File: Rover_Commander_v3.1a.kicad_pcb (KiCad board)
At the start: 2 copper layers, 77 x 42 mm, 73 parts, among them Q1 Crystal KX-7 25MHz, Q2 Crystal KX-7 25MHz, U1 RTL8201CP, U2 L7805ABD2T-TR, U3 H1102NLT, U4 LD1117S33TR_SOT223, U5 STM32F107RCTx, U6 TJA1040T, U7 M95160-WMN6TP

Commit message: fix swd connector, reversed GND and POWER +3.3V
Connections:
- XP2 pad 1: /+3V3_STM -> GND
- XP2 pad 4: GND -> /+3V3_STM
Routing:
- net GND: track 489.3 -> 497.2 mm, vias 13 -> 15
- net /+3V3_STM: track 79.9 -> 83.5 mm
- net (no net): vias 0 -> 1

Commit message: switch to my library https://github.com/Zulljon/zpkl.git
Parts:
- U2: footprint TO254P1542X460-3N -> zulljon:TO254P1542X460-3N
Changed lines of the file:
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@@
     )
   )
-  (module TO254P1542X460-3N (layer F.Cu)
+  (module zulljon:TO254P1542X460-3N (layer F.Cu)
     (at 127.712 115.316 180)
     (descr D2PAK_STD_ST)
     (tags "Integrated Circuit")
     (attr smd)
-    (fp_text reference U2 (at 0.712 6.316 180) (layer F.SilkS)
+    (fp_text reference U2 (at 0 0 180) (layer F.SilkS)
       (effects (font (size 1.27 1.27) (thickness 0.254)))
     )
@@
     (fp_line (start 0 0.5) (end 0 -0.5) (layer Dwgs.User) (width 0.05))
     (fp_line (start -0.5 0) (end 0.5 0) (layer Dwgs.User) (width 0.05))
-    (fp_line (start -2.708 5.1) (end 6.442 5.1) (layer Dwgs.User) (width 0.1))
-    (fp_line (start 6.442 5.1) (end 6.442 -5.1) (layer Dwgs.User) (width 0.1))
-    (fp_line (start 6.442 -5.1) (end -2.708 -5.1) (layer Dwgs.User) (width 0.1))
-    (fp_line (start -2.708 -5.1) (end -2.708 5.1) (layer Dwgs.User) (width 0.1))
-    (fp_line (start 6.442 5.1) (end 6.861 5.1) (layer Dwgs.User) (width 0.1))
-    (fp_line (start 6.861 5.1) (end 7.712 4.157) (layer Dwgs.User) (width 0.1))
-    (fp_line (start 7.712 4.157) (end 7.712 -4.157) (layer Dwgs.User) (width 0.1))
-    (fp_line (start 7.712 -4.157) (end 6.861 -5.1) (layer Dwgs.User) (width 0.1))
-    (fp_line (start 6.861 -5.1) (end 6.442 -5.1) (layer Dwgs.User) (width 0.1))
+    (fp_line (start -2.708 5.1) (end 6.442 5.1) (layer F.Fab) (width 0.1))
+    (fp_line (start 6.442 5.1) (end 6.442 -5.1) (layer F.Fab) (width 0.1))
+    (fp_line (start 6.442 -5.1) (end -2.708 -5.1) (layer F.Fab) (width 0.1))
+    (fp_line (start -2.708 -5.1) (end -2.708 5.1) (layer F.Fab) (width 0.1))
+    (fp_line (start 6.442 5.1) (end 6.861 5.1) (layer F.Fab) (width 0.1))
+    (fp_line (start 6.861 5.1) (end 7.712 4.157) (layer F.Fab) (width 0.1))
+    (fp_line (start 7.712 4.157) (end 7.712 -4.157) (layer F.Fab) (width 0.1))
+    (fp_line (start 7.712 -4.157) (end 6.861 -5.1) (layer F.Fab) (width 0.1))
+    (fp_line (start 6.861 -5.1) (end 6.442 -5.1) (layer F.Fab) (width 0.1))
     (fp_line (start -0.4 5.1) (end -4.1 5.1) (layer F.SilkS) (width 0.2))
     (fp_line (start -4.1 5.1) (end -4.1 -5.1) (layer F.SilkS) (width 0.2))

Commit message: add transient voltage suppression diods on CAN
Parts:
- added D7: SMAJ33CA-TR, Diodes_SMD:D_SMA, F.Cu at (114.5, 97.0)
- added D8: SMAJ33CA-TR, Diodes_SMD:D_SMA, F.Cu at (114.5, 104.5)
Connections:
- U1 pad 27: (no net) -> Net-(U1-Pad27)
- U5 pad 20: (no net) -> Net-(U5-Pad20)
- U5 pad 28: (no net) -> Net-(U5-Pad28)
- U5 pad 35: (no net) -> Net-(U5-Pad35)
- U5 pad 36: (no net) -> Net-(U5-Pad36)
- U5 pad 37: (no net) -> Net-(U5-Pad37)
- U5 pad 38: (no net) -> Net-(U5-Pad38)
- U5 pad 4: (no net) -> Net-(U5-Pad4)
- U5 pad 40: (no net) -> Net-(U5-Pad40)
- U5 pad 41: (no net) -> Net-(U5-Pad41)
- U5 pad 43: (no net) -> Net-(U5-Pad43)
- U5 pad 54: (no net) -> Net-(U5-Pad54)
- U5 pad 55: (no net) -> Net-(U5-Pad55)
- U5 pad 56: (no net) -> Net-(U5-Pad56)
- U5 pad 59: (no net) -> Net-(U5-Pad59)
- U5 pad 60: (no net) -> Net-(U5-Pad60)
- U5 pad 62: (no net) -> Net-(U5-Pad62)
- U5 pad 7: (no net) -> Net-(U5-Pad7)
- U5 pad 8: (no net) -> Net-(U5-Pad8)
- U7 pad 3: (no net) -> Net-(U7-Pad3)
- U7 pad 7: (no net) -> Net-(U7-Pad7)
- XP3 pad 9: (no net) -> /OBD2_ETH_ACT
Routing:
- net GND: track 497.2 -> 519.5 mm
- net /OBD2_CAN_H: track 6.88 -> 14.8 mm
- net /OBD2_CAN_L: track 13.1 -> 20.4 mm
- net Net-(C22-Pad1): track 24.3 -> 25.6 mm

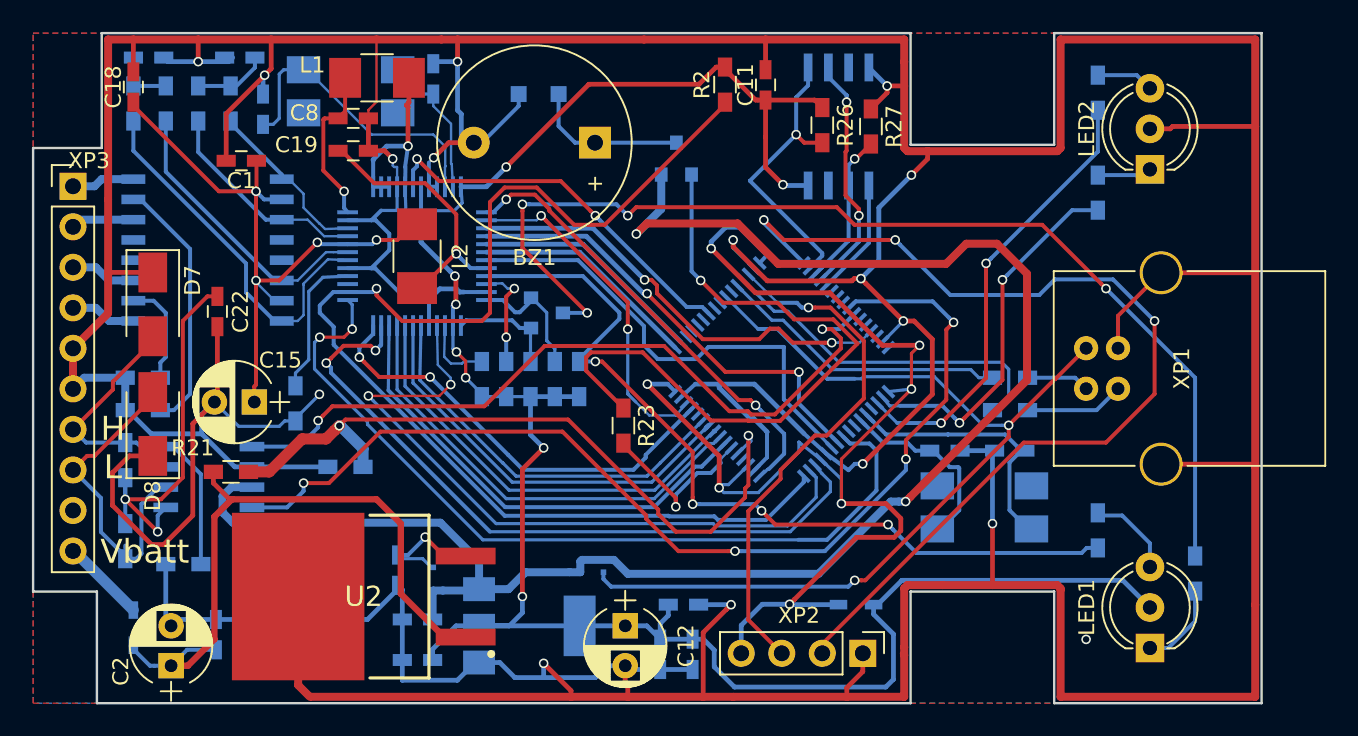
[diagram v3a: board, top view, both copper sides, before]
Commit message: fix crystals package, add thermo-pads to voltage regulator, fix usb like differential pair
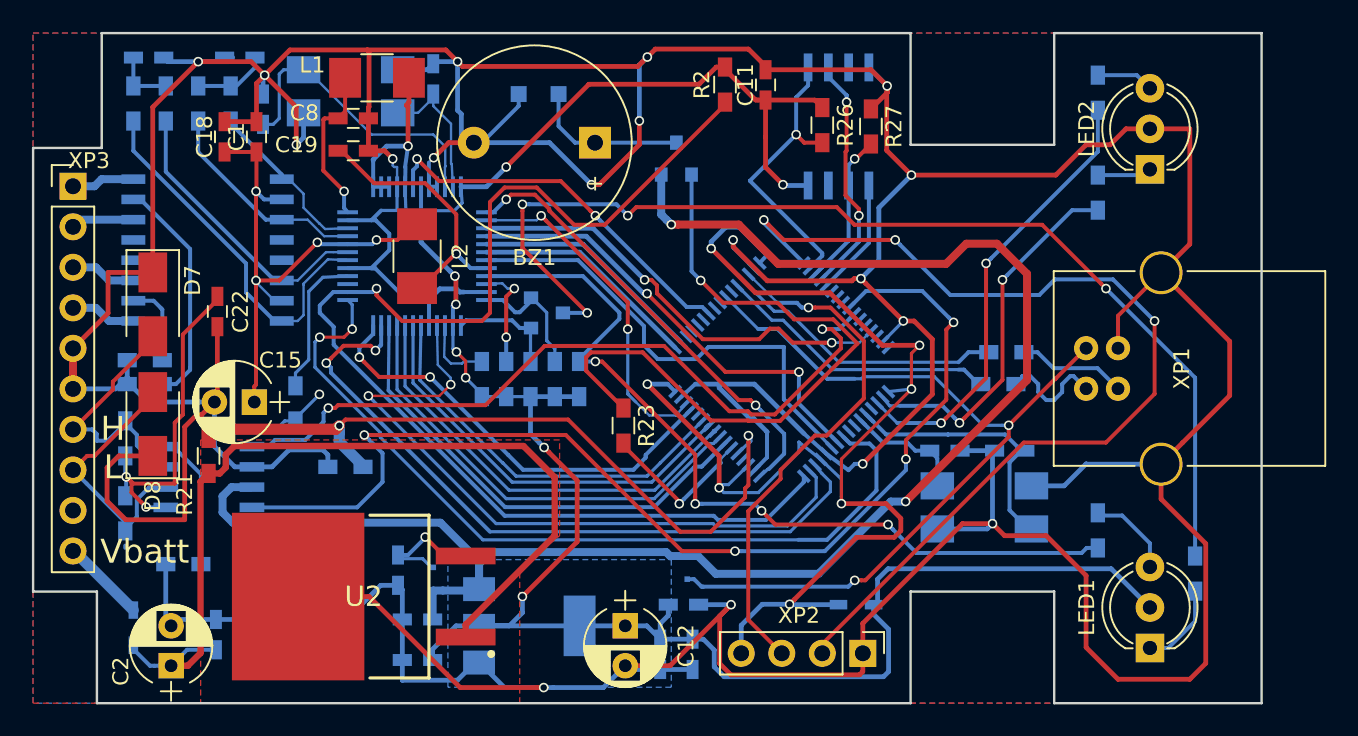
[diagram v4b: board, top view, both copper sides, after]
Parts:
- moved C18 6.51 mm to (119.0, 86.5)
- moved D4 5.98 mm to (148.0, 113.5), turned to 270 degrees
- moved R16 3.64 mm to (168.0, 100.0)
- moved C1 1.78 mm to (121.0, 86.5), turned to 90 degrees
- moved R25 1.74 mm to (112.8, 110.1)
- moved R21 1.72 mm to (118.0, 106.5), turned to 90 degrees
- moved R8 1.64 mm to (114.0, 102.0)
- moved R24 1.36 mm to (112.8, 105.4)
- moved R9 1.11 mm to (114.0, 100.5)
- moved R19 0.83 mm to (167.5, 102.0)
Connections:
- net Net-(R16-Pad1) renamed /USB_+
- net Net-(R19-Pad1) renamed /USB_-
- Q1 pad 2: Net-(C13-Pad1) -> GND
- Q1 pad 3: (no net) -> Net-(C13-Pad1)
- Q1 pad 4: (no net) -> GND
- Q2 pad 2: Net-(C21-Pad1) -> GND
- Q2 pad 3: (no net) -> Net-(C21-Pad1)
- Q2 pad 4: (no net) -> GND
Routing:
- net GND: track 519.5 -> 485.7 mm, vias 15 -> 19
- net /STM_ADC_12V: track 42.0 -> 55.9 mm
- net /TRANS_CT: track 41.0 -> 33.4 mm
- net /USB_Vbus: track 58.7 -> 53.0 mm
- net /USB_D+: track 22.1 -> 17.8 mm
- net Net-(C21-Pad1): track 12.0 -> 7.79 mm
- net Net-(C22-Pad1): track 25.6 -> 21.8 mm
- net /OBD2_CAN_L: track 20.4 -> 16.8 mm
- net /CAN_RX: track 66.4 -> 69.7 mm
- net /USB_-: track 3.95 -> 6.82 mm
- net /+5V: track 106.0 -> 103.4 mm
- net /+3V3_EEPROM: track 149.8 -> 151.8 mm
- net Net-(R8-Pad1): track 16.2 -> 14.5 mm
- net /OBD2_CAN_H: track 14.8 -> 16.4 mm
- net /ADC_Vbat: track 45.2 -> 46.6 mm
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- added copper zone on B.Cu, net /+3V3_EEPROM

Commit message: generate gerber files
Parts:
- moved R8 2.69 mm to (116.5, 103.0), turned to 270 degrees
- moved R9 2.55 mm to (114.5, 103.0), turned to 90 degrees
- moved R21 1.58 mm to (117.5, 108.0)
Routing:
- net GND: track 485.7 -> 502.2 mm, vias 19 -> 20
- net Net-(R23-Pad1): track 43.4 -> 40.1 mm
- net /ADC_Vbat: track 46.6 -> 48.4 mm
- net Net-(R9-Pad2): track 5.22 -> 6.90 mm
- net Net-(R8-Pad1): track 14.5 -> 13.1 mm
- net Net-(D3-Pad3): track 68.3 -> 69.7 mm
- net /TRANSF_TX+: track 11.4 -> 12.5 mm
- net /CAN_RX: track 69.7 -> 70.6 mm
- net /+3V3_EEPROM: track 151.8 -> 151.2 mm
- net Net-(R10-Pad2): track 52.8 -> 52.3 mm
- net /+3V3_STM: track 83.5 -> 82.9 mm
